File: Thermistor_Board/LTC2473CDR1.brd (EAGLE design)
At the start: 25.4 x 29.8 mm, 33 parts, among them J1 282834-4, J2 I2C, J3 I2C, J4 I2C, U1 LTC2473IMS#PBF, U2 LTC2473IMS#PBF

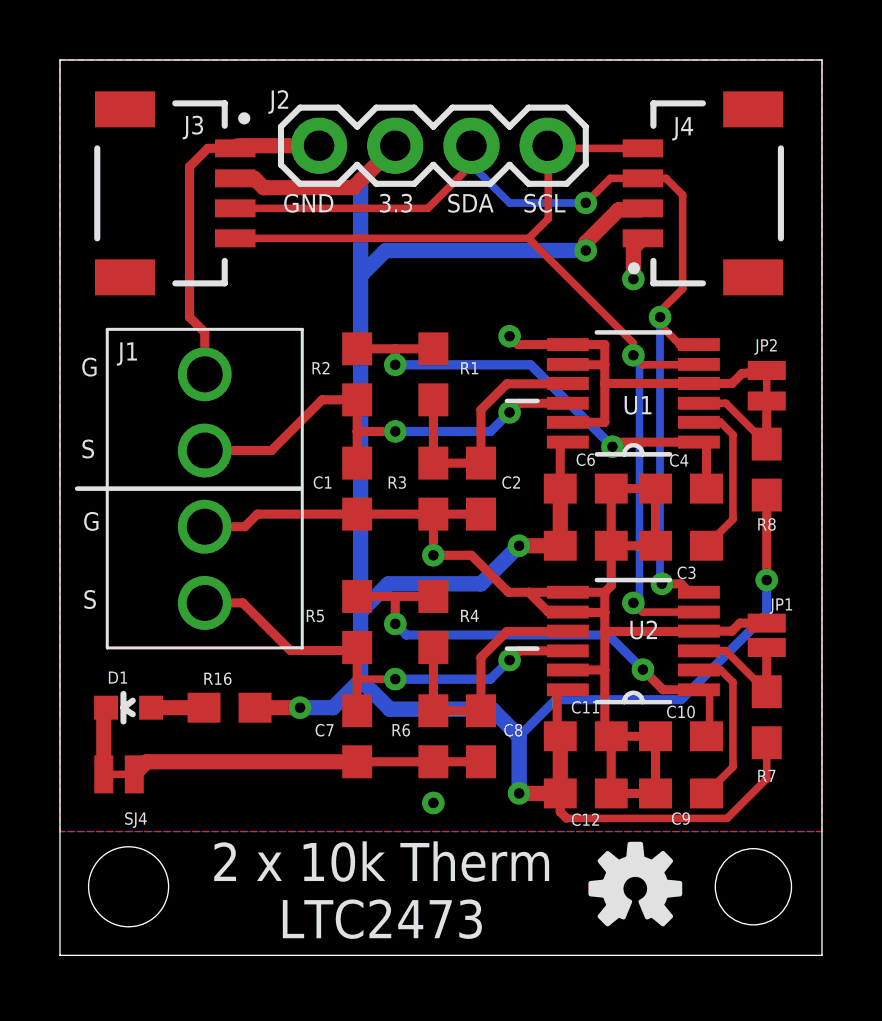
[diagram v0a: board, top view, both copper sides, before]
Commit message: Minor Updates LTC board
Silkscreen
Updates to via positions
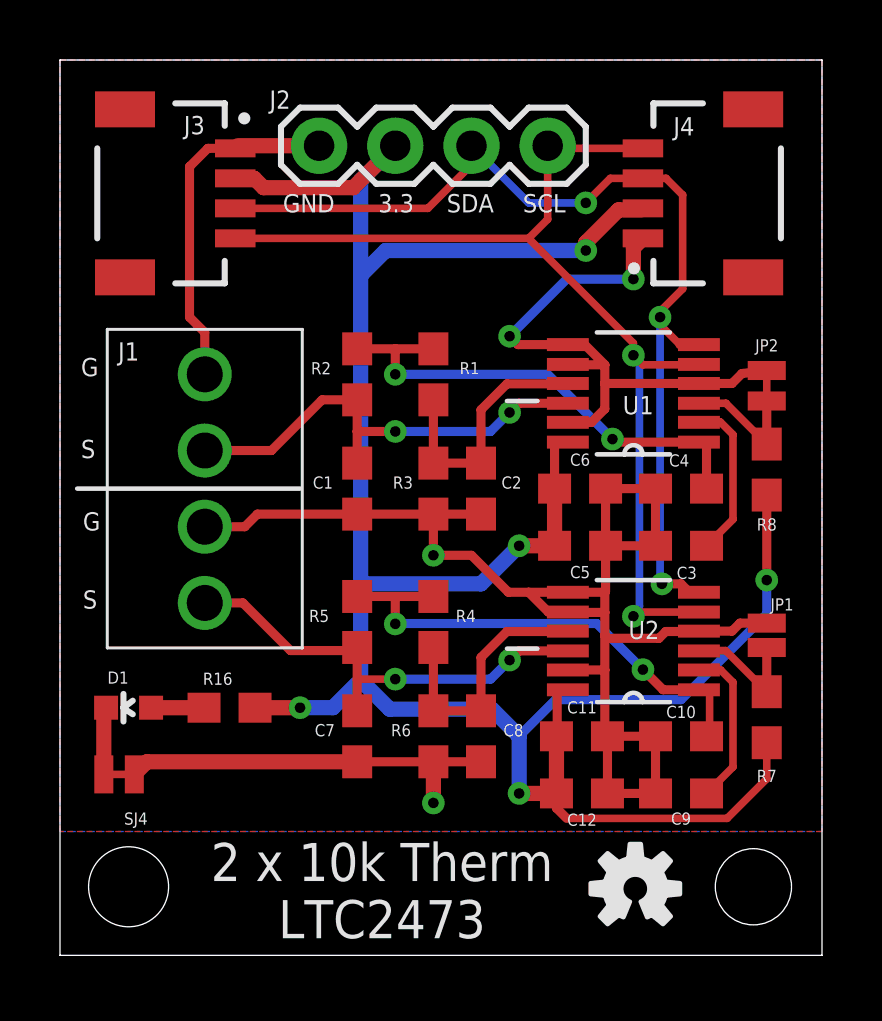
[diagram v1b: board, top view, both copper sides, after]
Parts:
- moved C5 0.19 mm to (17.3, 13.7)
- moved C6 0.19 mm to (17.3, 15.6)
- moved C11 0.13 mm to (17.4, 7.30)
- moved C12 0.13 mm to (17.4, 5.40)
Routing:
- net GND: track 86.5 -> 92.7 mm
